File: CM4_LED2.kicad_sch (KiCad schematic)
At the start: 2 parts

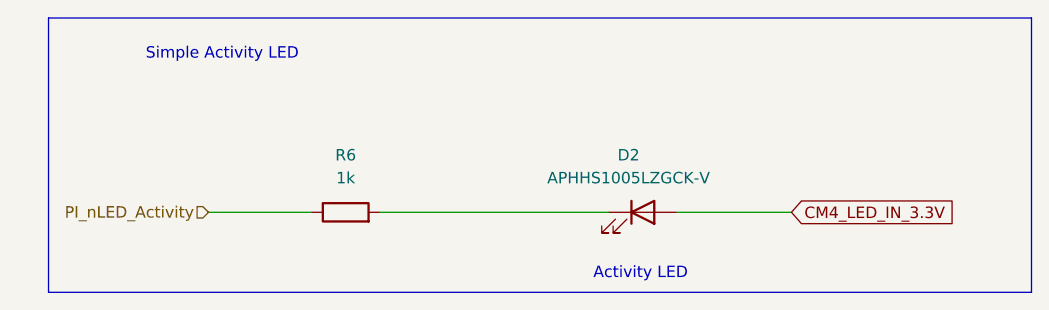
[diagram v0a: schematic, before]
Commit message: chore: multiple cosmetic wiring changes
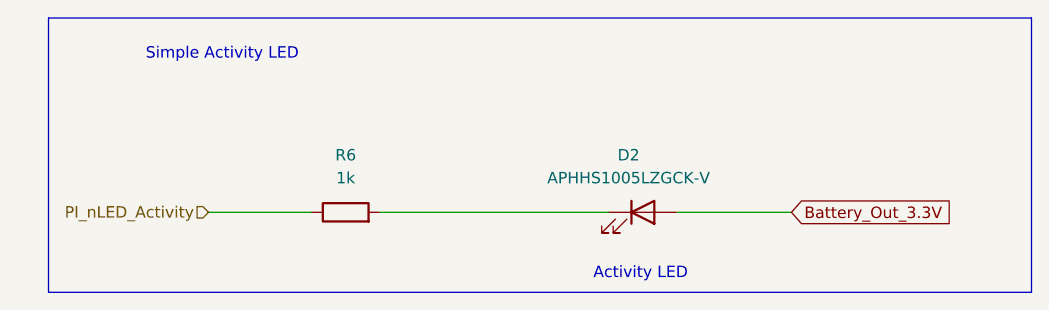
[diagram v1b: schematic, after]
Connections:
- net CM4_LED_IN_3.3V renamed Battery_Out_3.3V
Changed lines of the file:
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@@
 		)
 	)
-	(global_label "CM4_LED_IN_3.3V"
+	(global_label "Battery_Out_3.3V"
 		(shape input)
 		(at 135.89 62.23 0)
@@
 		)
 		(property "Intersheetrefs" "${INTERSHEET_REFS}"
-			(at 155.2037 62.23 0)
+			(at 154.8408 62.23 0)
 			(effects
 				(font

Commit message: chore: Many routing changes
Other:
- moved on the sheet: D2, R6
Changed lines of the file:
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@@
 	(text "Activity LED"
 		(exclude_from_sim no)
-		(at 119.126 69.088 0)
+		(at 91.694 69.088 0)
 		(effects
 			(font
@@
 	(wire
 		(pts
-			(xy 90.17 62.23) (xy 115.57 62.23)
+			(xy 120.65 62.23) (xy 95.25 62.23)
 		)
 		(stroke
@@
 	(wire
 		(pts
-			(xy 71.12 62.23) (xy 82.55 62.23)
+			(xy 139.7 62.23) (xy 128.27 62.23)
 		)
 		(stroke
@@
 	(wire
 		(pts
-			(xy 123.19 62.23) (xy 135.89 62.23)
+			(xy 87.63 62.23) (xy 74.93 62.23)
 		)
 		(stroke
@@
 		)
 	)
-	(global_label "Battery_Out_3.3V"
+	(hierarchical_label "PI_nLED_Activity"
 		(shape input)
-		(at 135.89 62.23 0)
-		(fields_autoplaced yes)
+		(at 139.7 62.23 0)
 		(effects
 			(font
@@
 			(justify left)
 		)
-		(property "Intersheetrefs" "${INTERSHEET_REFS}"
-			(at 154.8408 62.23 0)
-			(effects
-				(font
-					(size 1.27 1.27)
-				)
-				(justify left)
-				(hide yes)
-			)
-		)
-	)
-	(hierarchical_label "PI_nLED_Activity"
+	)
+	(hierarchical_label "Battery_Out_3.3V"
 		(shape input)
-		(at 71.12 62.23 180)
+		(at 74.93 62.23 180)
 		(effects
 			(font
@@
 	(symbol
 		(lib_id "#dzdb:g_res/R-1k-0603")
-		(at 86.36 62.23 90)
+		(at 124.46 62.23 270)
+		(mirror x)
 		(unit 1)
 		(exclude_from_sim no)
@@
 		(fields_autoplaced yes)
 		(property "Reference" "R6"
-			(at 86.36 55.88 90)
+			(at 124.46 55.88 90)
 			(effects
 				(font
@@
 		)
 		(property "Value" "1k"
-			(at 86.36 58.42 90)
+			(at 124.46 58.42 90)
 			(effects
 				(font
@@
 		)
 		(property "Footprint" "Resistor_SMD:R_0603_1608Metric"
-			(at 86.36 64.008 90)
+			(at 124.46 64.008 90)
 			(effects
 				(font
@@
 		)
 		(property "Datasheet" "https://www.we-online.com/components/products/datasheet/560112116014.pdf"
-			(at 86.36 62.23 0)
+			(at 124.46 62.23 0)
 			(effects
 				(font
@@
 		)
 		(property "Description" "Thick Film Resistors - SMD WRIS-RSKS 1 kOhms 1 % 0.1 W 0603"
-			(at 86.36 62.23 0)
+			(at 124.46 62.23 0)
 			(effects
 				(font
@@
 		)
 		(property "IPN" "R-1k-0603"
-			(at 86.36 62.23 0)
+			(at 124.46 62.23 0)
 			(effects
 				(font
@@
 		)
 		(property "MPN" "560112116014"
-			(at 86.36 62.23 0)
+			(at 124.46 62.23 0)
 			(effects
 				(font
@@
 		)
 		(property "Manufacturer" "Wurth Elektronik"
-			(at 86.36 62.23 0)
+			(at 124.46 62.23 0)
 			(effects
 				(font
@@
 		)
 		(property "Resistance" "1k"
-			(at 86.36 62.23 0)
+			(at 124.46 62.23 0)
 			(effects
 				(font
@@
 		)
 		(property "Power" "0.1 W"
-			(at 86.36 62.23 0)
+			(at 124.46 62.23 0)
 			(effects
 				(font
@@
 		)
 		(property "Material" "Thick film"
-			(at 86.36 62.23 0)
+			(at 124.46 62.23 0)
 			(effects
 				(font
@@
 		)
 		(property "Tolerance" "1 %"
-			(at 86.36 62.23 0)
+			(at 124.46 62.23 0)
 			(effects
 				(font
@@
 		)
 		(property "Supplier" "Mouser"
-			(at 86.36 62.23 0)
+			(at 124.46 62.23 0)
 			(effects
 				(font
@@
 		)
 		(property "SPN" "710-560112116014"
-			(at 86.36 62.23 0)
+			(at 124.46 62.23 0)
 			(effects
 				(font
@@
 		)
 		(property "LCSC" "CXXXXX"
-			(at 86.36 62.23 0)
+			(at 124.46 62.23 0)
 			(effects
 				(font
@@
 		)
 		(property "Comment" "lifecycle=Active; note=Auto-generated"
-			(at 86.36 62.23 0)
+			(at 124.46 62.23 0)
 			(effects
 				(font
@@
 	(symbol
 		(lib_id "#dzdb:s_dio/D-KIN-APHHS1005LZGCK-V")
-		(at 119.38 62.23 0)
+		(at 91.44 62.23 0)
+		(mirror y)
 		(unit 1)
 		(exclude_from_sim no)
@@
 		(fields_autoplaced yes)
 		(property "Reference" "D2"
-			(at 117.7925 55.88 0)
+			(at 93.0275 55.88 0)
 			(effects
 				(font
@@
 		)
 		(property "Value" "APHHS1005LZGCK-V"
-			(at 117.7925 58.42 0)
+			(at 93.0275 58.42 0)
 			(effects
 				(font
@@
 		)
 		(property "Footprint" "LED_SMD:LED_0402_1005Metric"
-			(at 119.38 62.23 0)
+			(at 91.44 62.23 0)
 			(effects
 				(font
@@
 		)
 		(property "Datasheet" "https://www.kingbrightusa.com/images/catalog/SPEC/APHHS1005LZGCK-V.pdf"
-			(at 119.38 62.23 0)
+			(at 91.44 62.23 0)
 			(effects
 				(font
@@
 		)
 		(property "Description" "LED EMERALD GREEN 525nm 180mcd@2mA 40mcd@0.44mA 2.54V"
-			(at 119.38 62.23 0)
+			(at 91.44 62.23 0)
 			(effects
 				(font
@@
 		)
 		(property "Sim.Pins" "1=K 2=A"
-			(at 119.38 62.23 0)
+			(at 91.44 62.23 0)
 			(effects
 				(font
@@
 		)
 		(property "IPN" "D-KIN-APHHS1005LZGCK-V"
-			(at 119.38 62.23 0)
+			(at 91.44 62.23 0)
 			(effects
 				(font
@@
 		)
 		(property "MPN" "APHHS1005LZGCK-V"
-			(at 119.38 62.23 0)
+			(at 91.44 62.23 0)
 			(effects
 				(font
@@
 		)
 		(property "Manufacturer" "Kingbright"
-			(at 119.38 62.23 0)
+			(at 91.44 62.23 0)
 			(effects
 				(font
@@
 		)
 		(property "Type" "LED GREEN"
-			(at 119.38 62.23 0)
+			(at 91.44 62.23 0)
 			(effects
 				(font
@@
 		)
 		(property "Vf" "2.65V"
-			(at 119.38 62.23 0)
+			(at 91.44 62.23 0)
 			(effects
 				(font
@@
 		)
 		(property "If" "2mA"
-			(at 119.38 62.23 0)
+			(at 91.44 62.23 0)
 			(effects
 				(font
@@
 		)
 		(property "Supplier" "Mouser"
-			(at 119.38 62.23 0)
+			(at 91.44 62.23 0)
 			(effects
 				(font
@@
 		)
 		(property "SPN" "604-APHHS1005LZGCK-V"
-			(at 119.38 62.23 0)
+			(at 91.44 62.23 0)
 			(effects
 				(font
@@
 		)
 		(property "LCSC" "C5875752"
-			(at 119.38 62.23 0)
+			(at 91.44 62.23 0)
 			(effects
 				(font
@@
 		)
 		(property "Comment" "lifecycle=Active"
-			(at 119.38 62.23 0)
-			(effects
-				(font
+			(at 91.44 62.23 0)
+			(effects
+				(font

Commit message: chore: more cleanup
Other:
- company: (none) -> Davide
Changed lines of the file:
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@@
 	(generator_version "9.0")
 	(paper "A4")
+	(title_block
+		(date "2025-11-18")
+		(company "Davide")
+	)
 	(rectangle
 		(start 53.34 40.64)

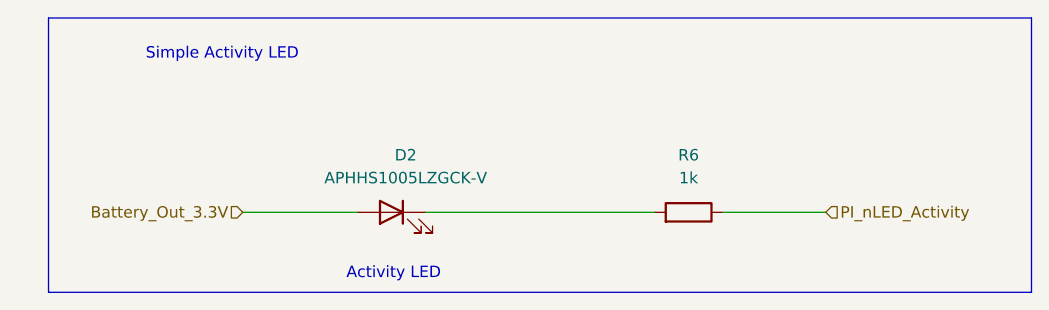
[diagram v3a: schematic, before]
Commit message: chore: added LED indicators for power and activity status, updated symbold, rerouted some things for better visibility
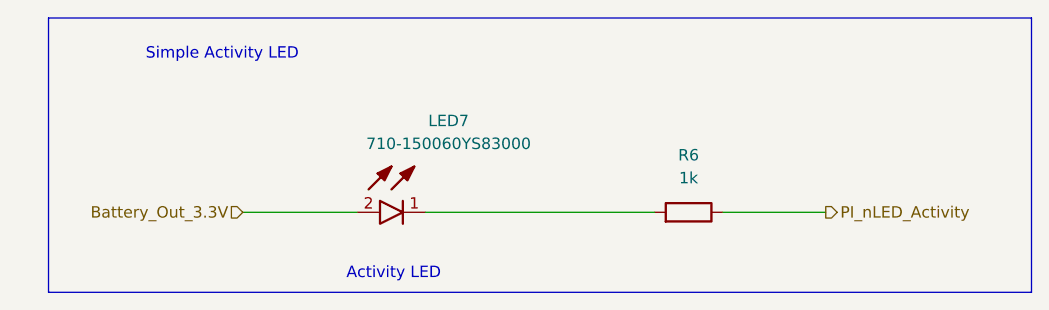
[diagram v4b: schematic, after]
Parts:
- removed D2: APHHS1005LZGCK-V, LED_SMD:LED_0402_1005Metric, symbol #dzdb:s_dio/D-KIN-APHHS1005LZGCK-V
- added LED7: 710-150060YS83000, dz_dio:Wuerth_LED_150060RS83000, symbol #dzdb:s_dio/D-WURT-710-150060YS83000
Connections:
- net Battery_Out_3.3V: now also LED7.2 (A)
- net at R6.2: now also LED7.1 (K)
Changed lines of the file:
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@@
 	(paper "A4")
 	(title_block
-		(date "2025-11-18")
+		(date "2025-11-19")
+		(rev "0")
 		(company "Davide")
 	)
@@
 	)
 	(hierarchical_label "PI_nLED_Activity"
-		(shape input)
+		(shape output)
 		(at 139.7 62.23 0)
 		(effects
@@
 	)
 	(symbol
-		(lib_id "#dzdb:s_dio/D-KIN-APHHS1005LZGCK-V")
+		(lib_id "#dzdb:s_dio/D-WURT-710-150060YS83000")
 		(at 91.44 62.23 0)
-		(mirror y)
 		(unit 1)
 		(exclude_from_sim no)
@@
 		(dnp no)
 		(fields_autoplaced yes)
-		(property "Reference" "D2"
-			(at 93.0275 55.88 0)
-			(effects
-				(font
-					(size 1.27 1.27)
-				)
-			)
-		)
-		(property "Value" "APHHS1005LZGCK-V"
-			(at 93.0275 58.42 0)
-			(effects
-				(font
-					(size 1.27 1.27)
-				)
-			)
-		)
-		(property "Footprint" "LED_SMD:LED_0402_1005Metric"
-			(at 91.44 62.23 0)
-			(effects
-				(font
-					(size 1.27 1.27)
-				)
-				(hide yes)
-			)
-		)
-		(property "Datasheet" "https://www.kingbrightusa.com/images/catalog/SPEC/APHHS1005LZGCK-V.pdf"
-			(at 91.44 62.23 0)
-			(effects
-				(font
-					(size 1.27 1.27)
-				)
-				(hide yes)
-			)
-		)
-		(property "Description" "LED EMERALD GREEN 525nm 180mcd@2mA 40mcd@0.44mA 2.54V"
-			(at 91.44 62.23 0)
-			(effects
-				(font
-					(size 1.27 1.27)
-				)
-				(hide yes)
-			)
-		)
-		(property "Sim.Pins" "1=K 2=A"
-			(at 91.44 62.23 0)
-			(effects
-				(font
-					(size 1.27 1.27)
-				)
-				(hide yes)
-			)
-		)
-		(property "IPN" "D-KIN-APHHS1005LZGCK-V"
-			(at 91.44 62.23 0)
-			(effects
-				(font
-					(size 1.27 1.27)
-				)
-				(hide yes)
-			)
-		)
-		(property "MPN" "APHHS1005LZGCK-V"
-			(at 91.44 62.23 0)
-			(effects
-				(font
-					(size 1.27 1.27)
-				)
-				(hide yes)
-			)
-		)
-		(property "Manufacturer" "Kingbright"
-			(at 91.44 62.23 0)
-			(effects
-				(font
-					(size 1.27 1.27)
-				)
-				(hide yes)
-			)
-		)
-		(property "Type" "LED GREEN"
-			(at 91.44 62.23 0)
-			(effects
-				(font
-					(size 1.27 1.27)
-				)
-				(hide yes)
-			)
-		)
-		(property "Vf" "2.65V"
-			(at 91.44 62.23 0)
-			(effects
-				(font
-					(size 1.27 1.27)
-				)
-				(hide yes)
-			)
-		)
-		(property "If" "2mA"
+		(property "Reference" "LED7"
+			(at 97.79 52.07 0)
+			(effects
+				(font
+					(size 1.27 1.27)
+				)
+			)
+		)
+		(property "Value" "710-150060YS83000"
+			(at 97.79 54.61 0)
+			(effects
+				(font
+					(size 1.27 1.27)
+				)
+			)
+		)
+		(property "Footprint" "dz_dio:Wuerth_LED_150060RS83000"
+			(at 104.14 155.88 0)
+			(effects
+				(font
+					(size 1.27 1.27)
+				)
+				(justify left bottom)
+				(hide yes)
+			)
+		)
+		(property "Datasheet" "https://www.we-online.com/catalog/datasheet/150060SY83000.pdf"
+			(at 104.14 255.88 0)
+			(effects
+				(font
+					(size 1.27 1.27)
+				)
+				(justify left bottom)
+				(hide yes)
+			)
+		)
+		(property "Description" "Einfarbige LEDs leds WL-SMCW SMT 0603 Dome Yellow Typ 650mcd 2V"
+			(at 91.44 62.23 0)
+			(effects
+				(font
+					(size 1.27 1.27)
+				)
+				(hide yes)
+			)
+		)
+		(property "Height" "0.95"
+			(at 104.14 455.88 0)
+			(effects
+				(font
+					(size 1.27 1.27)
+				)
+				(justify left bottom)
+				(hide yes)
+			)
+		)
+		(property "Mouser Part Number" ""
+			(at 104.14 555.88 0)
+			(effects
+				(font
+					(size 1.27 1.27)
+				)
+				(justify left bottom)
+				(hide yes)
+			)
+		)
+		(property "Mouser Price/Stock" ""
+			(at 104.14 655.88 0)
+			(effects
+				(font
+					(size 1.27 1.27)
+				)
+				(justify left bottom)
+				(hide yes)
+			)
+		)
+		(property "Manufacturer_Name" "Wurth Elektronik"
+			(at 104.14 755.88 0)
+			(effects
+				(font
+					(size 1.27 1.27)
+				)
+				(justify left bottom)
+				(hide yes)
+			)
+		)
+		(property "Manufacturer_Part_Number" "150060RS83000"
+			(at 104.14 855.88 0)
+			(effects
+				(font
+					(size 1.27 1.27)
+				)
+				(justify left bottom)
+				(hide yes)
+			)
+		)
+		(property "IPN" "D-WURT-710-150060YS83000"
+			(at 91.44 62.23 0)
+			(effects
+				(font
+					(size 1.27 1.27)
+				)
+				(hide yes)
+			)
+		)
+		(property "MPN" "710-150060YS83000"
+			(at 91.44 62.23 0)
+			(effects
+				(font
+					(size 1.27 1.27)
+				)
+				(hide yes)
+			)
+		)
+		(property "Manufacturer" "Wurth Elektronik"
+			(at 91.44 62.23 0)
+			(effects
+				(font
+					(size 1.27 1.27)
+				)
+				(hide yes)
+			)
+		)
+		(property "Type" "Einfarbige LEDs leds"
+			(at 91.44 62.23 0)
+			(effects
+				(font
+					(size 1.27 1.27)
+				)
+				(hide yes)
+			)
+		)
+		(property "Vf" "2V"
+			(at 91.44 62.23 0)
+			(effects
+				(font
+					(size 1.27 1.27)
+				)
+				(hide yes)
+			)
+		)
+		(property "If" "20 mA"
 			(at 91.44 62.23 0)
 			(effects
@@
 			)
 		)
-		(property "SPN" "604-APHHS1005LZGCK-V"
-			(at 91.44 62.23 0)
-			(effects
-				(font
-					(size 1.27 1.27)
-				)
-				(hide yes)
-			)
-		)
-		(property "LCSC" "C5875752"
-			(at 91.44 62.23 0)
-			(effects
-				(font
-					(size 1.27 1.27)
-				)
-				(hide yes)
-			)
-		)
-		(property "Comment" "lifecycle=Active"
-			(at 91.44 62.23 0)
-			(effects
-				(font
-					(size 1.27 1.27)
-				)
-				(hide yes)
-			)
+		(property "SPN" "710-150060YS83000"
+			(at 91.44 62.23 0)
+			(effects
+				(font
+					(size 1.27 1.27)
+				)
+				(hide yes)
+			)
+		)
+		(property "LCSC" ""
+			(at 91.44 62.23 0)
+			(effects
+				(font
+					(size 1.27 1.27)
+				)
+				(hide yes)
+			)
+		)
+		(property "Comment" "lifecycle=New Product"
+			(at 91.44 62.23 0)
+			(effects
+				(font
+					(size 1.27 1.27)
+				)
+				(hide yes)
+			)
+		)
+		(pin "2"
 		)
 		(pin "1"
 		)
-		(pin "2"
-		)
 		(instances
-			(project "nautilus_mainboard"
+			(project ""
 				(path "/ce1819b2-f280-40ed-834f-6fe4d12f809d/c2b6dac3-d6fd-4d5d-bd17-0cff91db88eb/0837dad1-ec16-488a-a684-981e55247089/b50f6d86-4325-4d05-931a-73973954b099"
-					(reference "D2")
+					(reference "LED7")
 					(unit 1)
 				)

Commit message: chore: Loads of redoing stuff. Added a Changelog
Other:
- title: (none) -> Nautilus_Mainboard
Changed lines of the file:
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@@
 	(paper "A4")
 	(title_block
+		(title "Nautilus_Mainboard")
 		(date "2025-11-19")
 		(rev "0")
